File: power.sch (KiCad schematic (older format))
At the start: 4 parts, among them U1 SP6205EM5-L-3-3_TR

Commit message: added power
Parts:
- added C? (x2): C, symbol Device:C
- added R?: 33R, symbol Device:R
- added R?: R, symbol Device:R
- C? (x2): value C -> 10nF
- R?: value R -> 100k
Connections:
- net labels added: +2V5
- wire segments 15 -> 27
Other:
- moved on the sheet: C?
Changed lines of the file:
@@
 F 3 "" H 3100 1750 50  0001 C CNN
 	1    3100 1750
-	0    1    1    0
+	1    0    0    -1
 $EndComp
 Wire Wire Line
@@
 	0    1    1    0
 $EndComp
-$Comp
-L Device:C C?
-U 1 1 5F46CE59
-P 5550 1900
-F 0 "C?" H 5665 1946 50  0000 L CNN
-F 1 "C" H 5665 1855 50  0000 L CNN
-F 2 "" H 5588 1750 50  0001 C CNN
-F 3 "~" H 5550 1900 50  0001 C CNN
-	1    5550 1900
-	1    0    0    -1
-$EndComp
-$Comp
-L Device:C C?
-U 1 1 5F46E13B
-P 5800 1900
-F 0 "C?" H 5915 1946 50  0000 L CNN
-F 1 "C" H 5915 1855 50  0000 L CNN
-F 2 "" H 5838 1750 50  0001 C CNN
-F 3 "~" H 5800 1900 50  0001 C CNN
-	1    5800 1900
-	1    0    0    -1
-$EndComp
-Wire Wire Line
-	5100 1750 5550 1750
+Wire Wire Line
+	5100 1750 5400 1750
 $Comp
 L power:GND #PWR?
@@
 $EndComp
 Wire Wire Line
-	5550 2050 5650 2050
-Wire Wire Line
 	5650 2050 5650 2250
 Wire Wire Line
 	5800 2050 5650 2050
-Connection ~ 5650 2050
 Wire Wire Line
 	5800 1750 5800 1650
@@
 P 3950 2350
 F 0 "R?" V 3743 2350 50  0000 C CNN
-F 1 "R" V 3834 2350 50  0000 C CNN
+F 1 "100k" V 3834 2350 50  0000 C CNN
 F 2 "" V 3880 2350 50  0001 C CNN
 F 3 "~" H 3950 2350 50  0001 C CNN
@@
 Wire Wire Line
 	2800 2350 3800 2350
+$Comp
+L Device:C C?
+U 1 1 5F46E13B
+P 5800 1900
+F 0 "C?" H 5915 1946 50  0000 L CNN
+F 1 "10nF" H 5915 1855 50  0000 L CNN
+F 2 "" H 5838 1750 50  0001 C CNN
+F 3 "~" H 5800 1900 50  0001 C CNN
+	1    5800 1900
+	1    0    0    -1
+$EndComp
+Connection ~ 5650 2050
+$Comp
+L Device:C C?
+U 1 1 5F46CE59
+P 5400 1900
+F 0 "C?" H 5515 1946 50  0000 L CNN
+F 1 "10nF" H 5515 1855 50  0000 L CNN
+F 2 "" H 5438 1750 50  0001 C CNN
+F 3 "~" H 5400 1900 50  0001 C CNN
+	1    5400 1900
+	1    0    0    -1
+$EndComp
+Wire Wire Line
+	5400 2050 5650 2050
+$Comp
+L power:GND #PWR?
+U 1 1 5F4AC863
+P 2800 1150
+F 0 "#PWR?" H 2800 900 50  0001 C CNN
+F 1 "GND" H 2805 977 50  0000 C CNN
+F 2 "" H 2800 1150 50  0001 C CNN
+F 3 "" H 2800 1150 50  0001 C CNN
+	1    2800 1150
+	-1   0    0    1
+$EndComp
+$Comp
+L Device:C C?
+U 1 1 5F4ACF4B
+P 2800 1400
+F 0 "C?" H 2915 1446 50  0000 L CNN
+F 1 "C" H 2915 1355 50  0000 L CNN
+F 2 "" H 2838 1250 50  0001 C CNN
+F 3 "~" H 2800 1400 50  0001 C CNN
+	1    2800 1400
+	1    0    0    -1
+$EndComp
+Wire Wire Line
+	2800 1550 2800 1650
+Wire Wire Line
+	2800 1250 2800 1150
+$Comp
+L power:+3.3V #PWR?
+U 1 1 5F4AF21A
+P 7750 1550
+F 0 "#PWR?" H 7750 1400 50  0001 C CNN
+F 1 "+3.3V" V 7765 1678 50  0000 L CNN
+F 2 "" H 7750 1550 50  0001 C CNN
+F 3 "" H 7750 1550 50  0001 C CNN
+	1    7750 1550
+	0    -1   -1   0
+$EndComp
+$Comp
+L Device:R R?
+U 1 1 5F4AF6DD
+P 8200 1550
+F 0 "R?" V 7993 1550 50  0000 C CNN
+F 1 "33R" V 8084 1550 50  0000 C CNN
+F 2 "" V 8130 1550 50  0001 C CNN
+F 3 "~" H 8200 1550 50  0001 C CNN
+	1    8200 1550
+	0    1    1    0
+$EndComp
+Wire Wire Line
+	7750 1550 8050 1550
+$Comp
+L power:GND #PWR?
+U 1 1 5F4AFAB4
+P 8500 2000
+F 0 "#PWR?" H 8500 1750 50  0001 C CNN
+F 1 "GND" H 8505 1827 50  0000 C CNN
+F 2 "" H 8500 2000 50  0001 C CNN
+F 3 "" H 8500 2000 50  0001 C CNN
+	1    8500 2000
+	1    0    0    -1
+$EndComp
+$Comp
+L Device:R R?
+U 1 1 5F4B1155
+P 8500 1750
+F 0 "R?" H 8570 1796 50  0000 L CNN
+F 1 "R" H 8570 1705 50  0000 L CNN
+F 2 "" V 8430 1750 50  0001 C CNN
+F 3 "~" H 8500 1750 50  0001 C CNN
+	1    8500 1750
+	1    0    0    -1
+$EndComp
+$Comp
+L Device:C C?
+U 1 1 5F4B14D7
+P 8850 1750
+F 0 "C?" H 8965 1796 50  0000 L CNN
+F 1 "C" H 8965 1705 50  0000 L CNN
+F 2 "" H 8888 1600 50  0001 C CNN
+F 3 "~" H 8850 1750 50  0001 C CNN
+	1    8850 1750
+	1    0    0    -1
+$EndComp
+Wire Wire Line
+	8350 1550 8500 1550
+Wire Wire Line
+	8500 1550 8500 1600
+Wire Wire Line
+	8850 1600 8850 1550
+Wire Wire Line
+	8850 1550 8500 1550
+Connection ~ 8500 1550
+Wire Wire Line
+	8500 1900 8500 1950
+Wire Wire Line
+	8850 1900 8850 1950
+Wire Wire Line
+	8850 1950 8500 1950
+Connection ~ 8500 1950
+Wire Wire Line
+	8500 1950 8500 2000
+$Comp
+L power:+2V5 #PWR?
+U 1 1 5F4B25FE
+P 9250 1550
+F 0 "#PWR?" H 9250 1400 50  0001 C CNN
+F 1 "+2V5" V 9265 1678 50  0000 L CNN
+F 2 "" H 9250 1550 50  0001 C CNN
+F 3 "" H 9250 1550 50  0001 C CNN
+	1    9250 1550
+	0    1    1    0
+$EndComp
+Wire Wire Line
+	8850 1550 9250 1550
+Connection ~ 8850 1550
 $EndSCHEMATC

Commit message: added more PowerSuply stuffs
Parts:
- removed U1: SP6205EM5-L-3-3_TR, SOT-23-5_VAR-AA, symbol SP6205EM5-L-3-3/TR:SP6205EM5-L-3-3_TR
- added C? (x5): 100nF, symbol Device:C
- added C?: 10nF, symbol Device:C
- added C?: 10uF, symbol Device:C
- added C? (x3): 22uF, symbol Device:CP1
- added C?: 1uF, symbol Device:C
- added L?: 3.3uH, symbol Device:L_Core_Iron
- added L?: 100r, symbol Device:L
- added R? (x4): 100K, symbol Device:R
- added R?: 20K, symbol Device:R
- added R?: 47K, symbol Device:R
- added U?: SP6205EM5-L-3-3_TR, SOT-23-5_VAR-AA, symbol Csky:SP6205EM5-L-3-3_TR
- C?: value C -> 10uF
- R?: value R -> 1K
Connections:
- net labels added: +1V0, +1V1, +1V8, MR, NRST_GX_CPU, VDD33
- wire segments 27 -> 110
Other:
- note added: "GPU Vcc\n"
- note added: "GX6605"
- note added: "GX6605S\nInternal DDR2"
- note added: "HDMI\n"
- note added: "ICE\nIO"
- note added: "Reset circuit"
- note added: "SPX3819-1.8\n"
- note added: "Vout=((R6/R9)+1)*0.8\n=((20/47)+1)*0.8=1.14V\n"
- moved on the sheet: C?

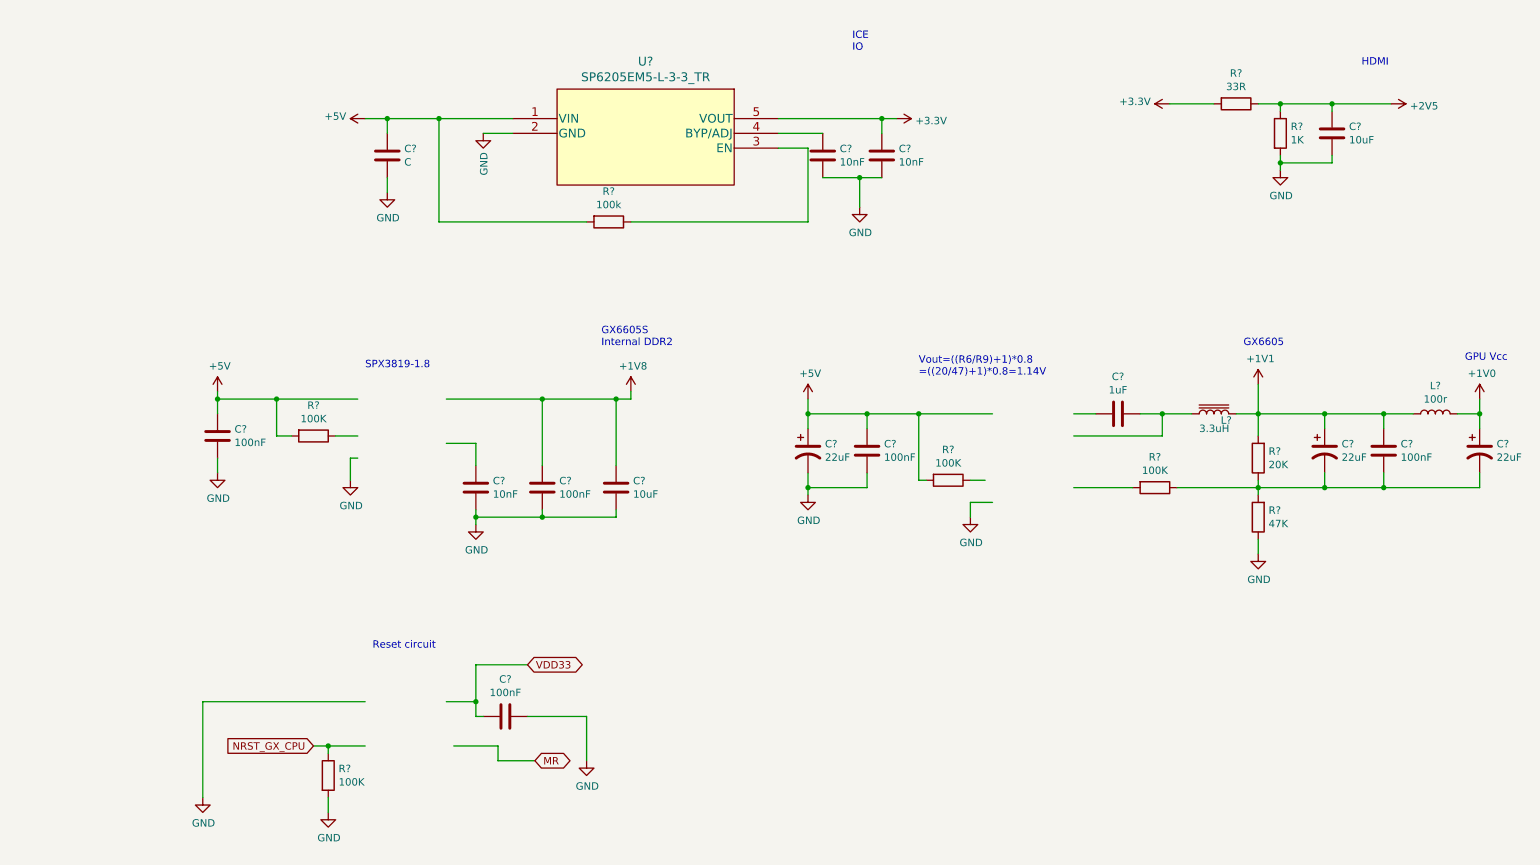
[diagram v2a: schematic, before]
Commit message: added sybmols for power stuff, and finished circuit
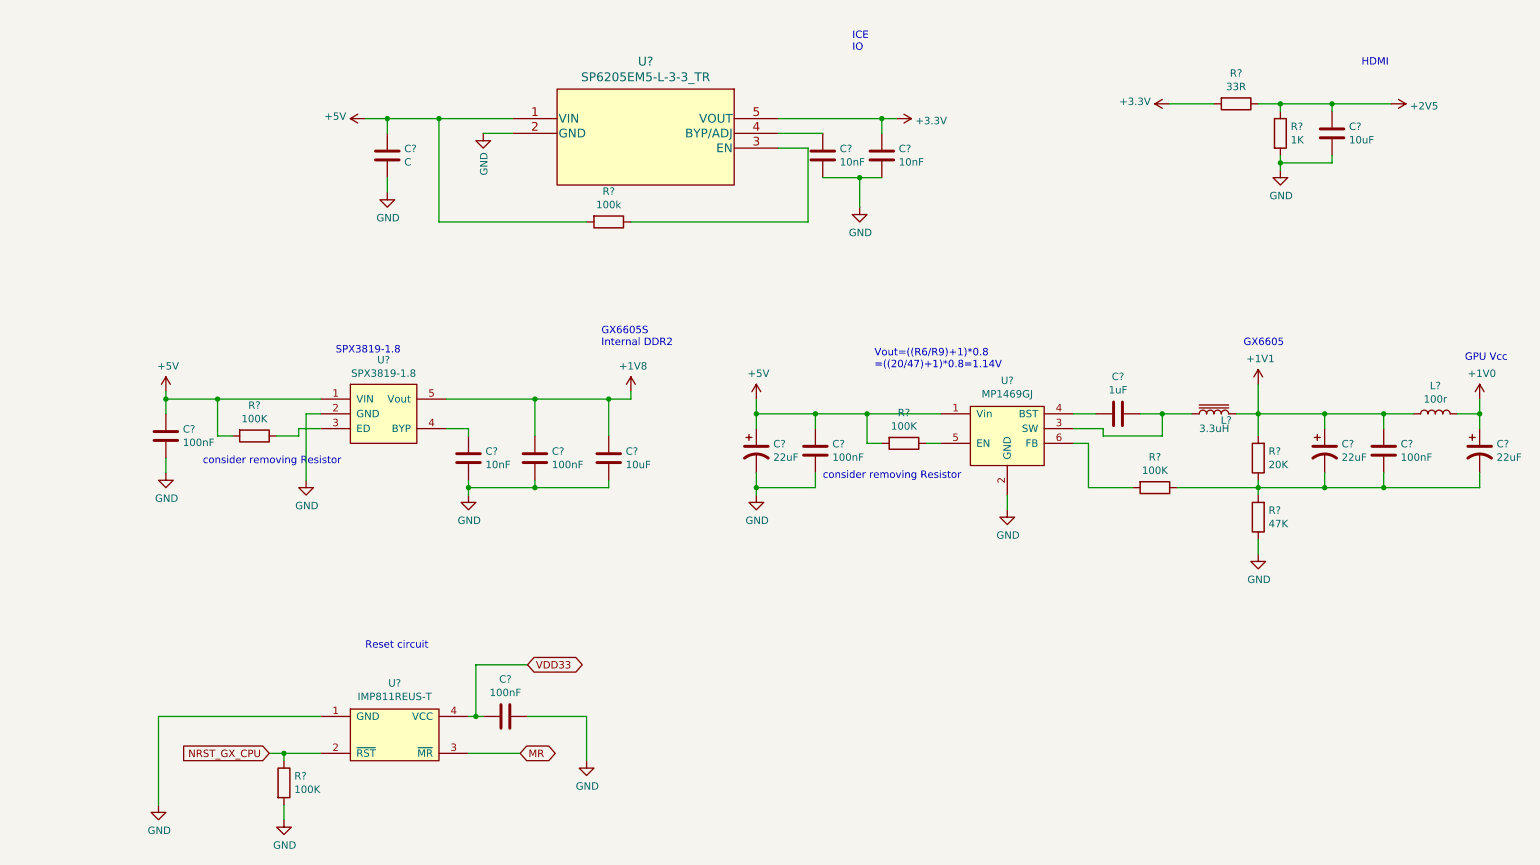
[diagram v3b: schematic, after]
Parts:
- added U?: IMP811REUS-T, symbol Csky:IMP811REUS-T
- added U?: SPX3819-1.8, symbol Csky:SPX3819-1.8
- added U?: MP1469GJ, symbol Csky:MP1469GJ
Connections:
- wire segments 110 -> 112
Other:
- note added: "consider removing Resistor"
- moved on the sheet: C?, R?

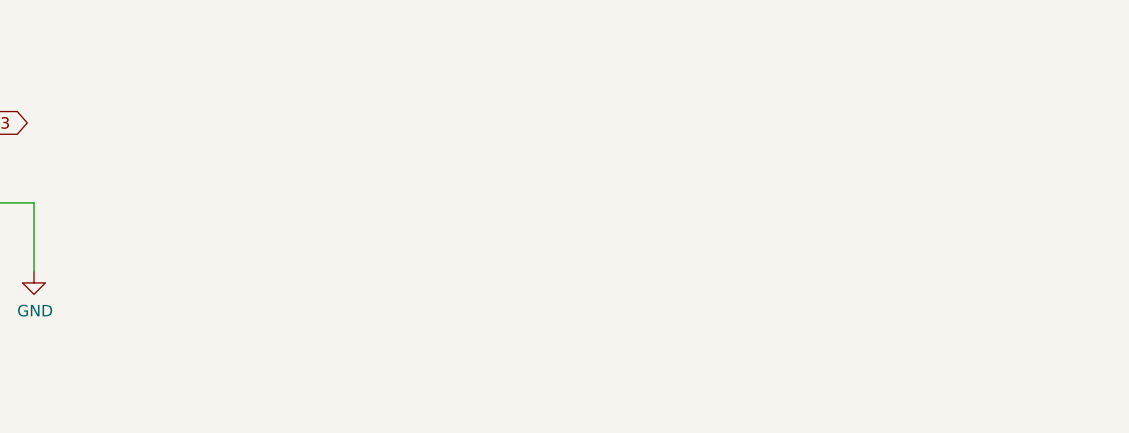
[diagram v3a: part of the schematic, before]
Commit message: added sheeT for CPU
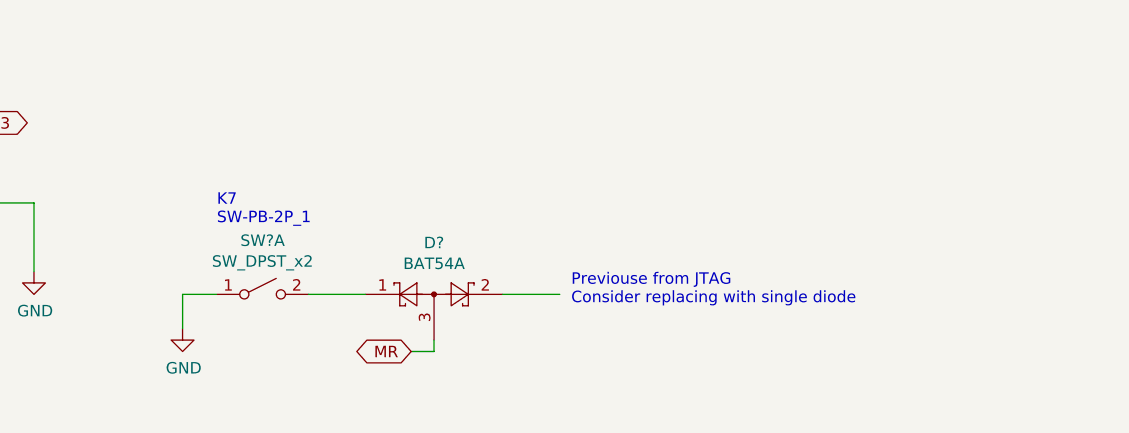
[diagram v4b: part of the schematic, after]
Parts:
- added D?: BAT54A, Package_TO_SOT_SMD:SOT-23, symbol Diode:BAT54A
- added SW?: SW_DPST_x2, symbol Switch:SW_DPST_x2
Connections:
- net GND: now also SW?.1 (A)
- net MR: now also D?.3
- new net: D?.1, SW?.2 (B)
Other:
- note added: "K7\nSW-PB-2P_1\n"
- note added: "Previouse from JTAG\nConsider replacing with single diode"
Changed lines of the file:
@@
 $Descr A4 11693 8268
 encoding utf-8
-Sheet 2 2
+Sheet 2 3
 Title ""
 Date ""
@@
 Wire Wire Line
 	5700 3650 6200 3650
+$Comp
+L Diode:BAT54A D?
+U 1 1 5F4AB793
+P 5550 6100
+F 0 "D?" H 5550 6325 50  0000 C CNN
+F 1 "BAT54A" H 5550 6234 50  0000 C CNN
+F 2 "Package_TO_SOT_SMD:SOT-23" H 5625 6225 50  0001 L CNN
+F 3 "http://www.diodes.com/_files/datasheets/ds11005.pdf" H 5430 6100 50  0001 C CNN
+	1    5550 6100
+	1    0    0    -1
+$EndComp
+Text GLabel 5450 6350 0    50   BiDi ~ 0
+MR
+Wire Wire Line
+	5450 6350 5550 6350
+Wire Wire Line
+	5550 6350 5550 6300
+Wire Wire Line
+	5850 6100 6100 6100
+$Comp
+L Switch:SW_DPST_x2 SW?
+U 1 1 5F4B482F
+P 4800 6100
+F 0 "SW?" H 4800 6335 50  0000 C CNN
+F 1 "SW_DPST_x2" H 4800 6244 50  0000 C CNN
+F 2 "" H 4800 6100 50  0001 C CNN
+F 3 "~" H 4800 6100 50  0001 C CNN
+	1    4800 6100
+	1    0    0    -1
+$EndComp
+$Comp
+L power:GND #PWR?
+U 1 1 5F4B4E43
+P 4450 6250
+F 0 "#PWR?" H 4450 6000 50  0001 C CNN
+F 1 "GND" H 4455 6077 50  0000 C CNN
+F 2 "" H 4450 6250 50  0001 C CNN
+F 3 "" H 4450 6250 50  0001 C CNN
+	1    4450 6250
+	1    0    0    -1
+$EndComp
+Wire Wire Line
+	4450 6250 4450 6100
+Wire Wire Line
+	4450 6100 4600 6100
+Wire Wire Line
+	5000 6100 5250 6100
+Text Notes 4600 5800 0    50   ~ 0
+K7\nSW-PB-2P_1\n
+Text Notes 6150 6150 0    50   ~ 0
+Previouse from JTAG\nConsider replacing with single diode
 $EndSCHEMATC

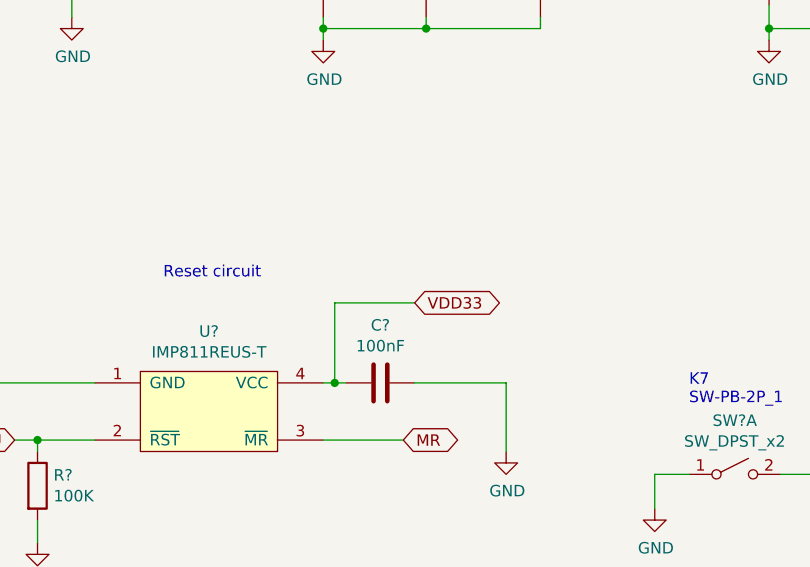
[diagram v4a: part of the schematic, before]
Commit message: added power to CPU
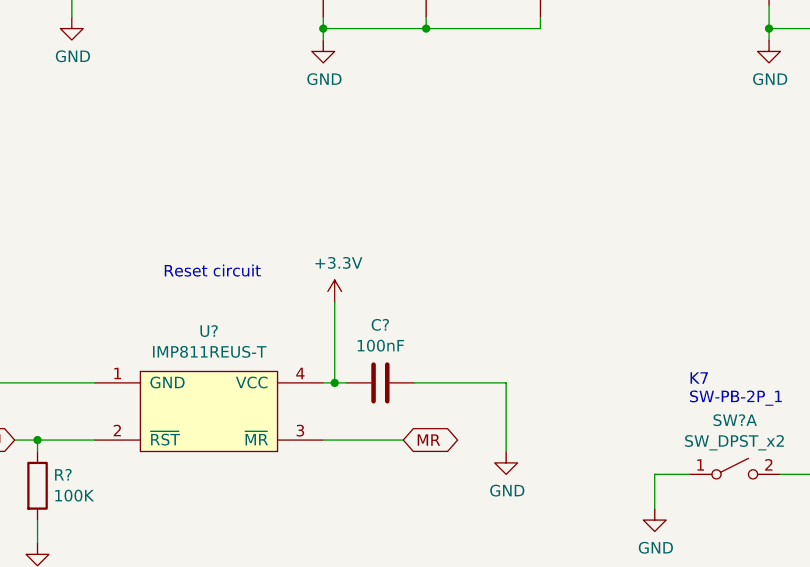
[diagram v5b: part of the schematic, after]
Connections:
- net VDD33 is gone; now on net +3V3: C?.2, U?.4 (VCC)
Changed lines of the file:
@@
 Wire Wire Line
 	3100 5700 3050 5700
-Wire Wire Line
-	3050 5350 3400 5350
-Text GLabel 3400 5350 2    50   BiDi ~ 0
-VDD33
 $Comp
 L power:GND #PWR?
@@
 Text Notes 6150 6150 0    50   ~ 0
 Previouse from JTAG\nConsider replacing with single diode
+$Comp
+L power:+3.3V #PWR?
+U 1 1 5F4DE606
+P 3050 5350
+F 0 "#PWR?" H 3050 5200 50  0001 C CNN
+F 1 "+3.3V" H 3065 5523 50  0000 C CNN
+F 2 "" H 3050 5350 50  0001 C CNN
+F 3 "" H 3050 5350 50  0001 C CNN
+	1    3050 5350
+	1    0    0    -1
+$EndComp
 $EndSCHEMATC

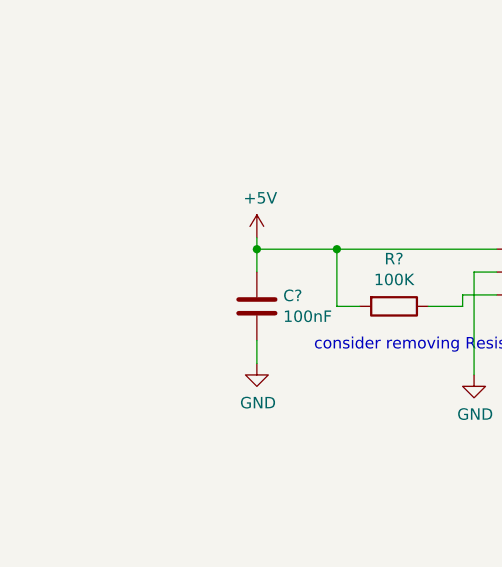
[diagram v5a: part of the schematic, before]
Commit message: wired SPI flash to cpu, and added CPU lables
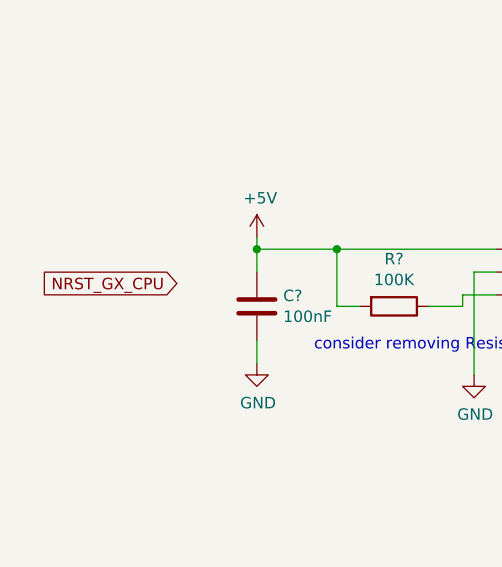
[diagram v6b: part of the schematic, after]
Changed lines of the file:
@@
 	1    0    0    -1
 $EndComp
+Text GLabel 600  3700 0    50   Input ~ 0
+NRST_GX_CPU
 $EndSCHEMATC
